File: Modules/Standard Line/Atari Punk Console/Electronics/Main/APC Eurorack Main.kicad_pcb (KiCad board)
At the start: 2 copper layers, 26 x 110 mm, 24 parts, among them IC1 78L05, IC2 LM556, J1 Power, J4 CV2, J5 Out, J6 CV1

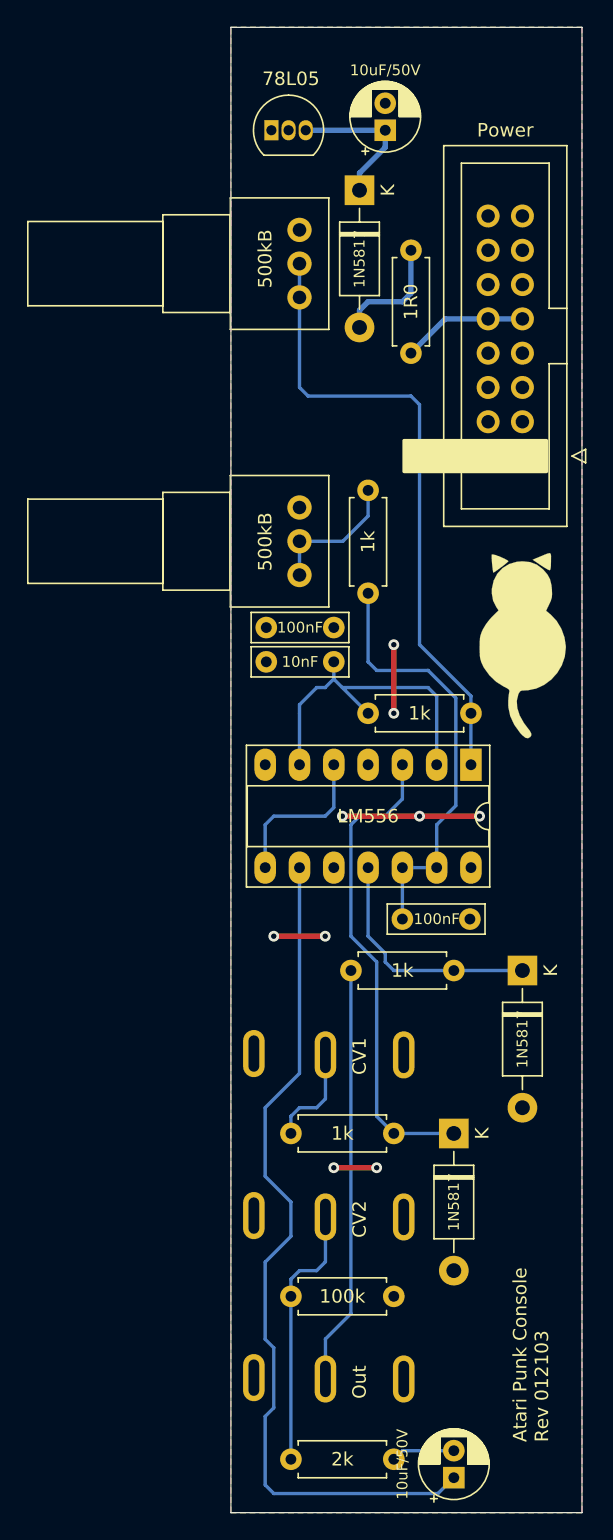
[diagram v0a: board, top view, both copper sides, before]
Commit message: 4Ch Mixer added
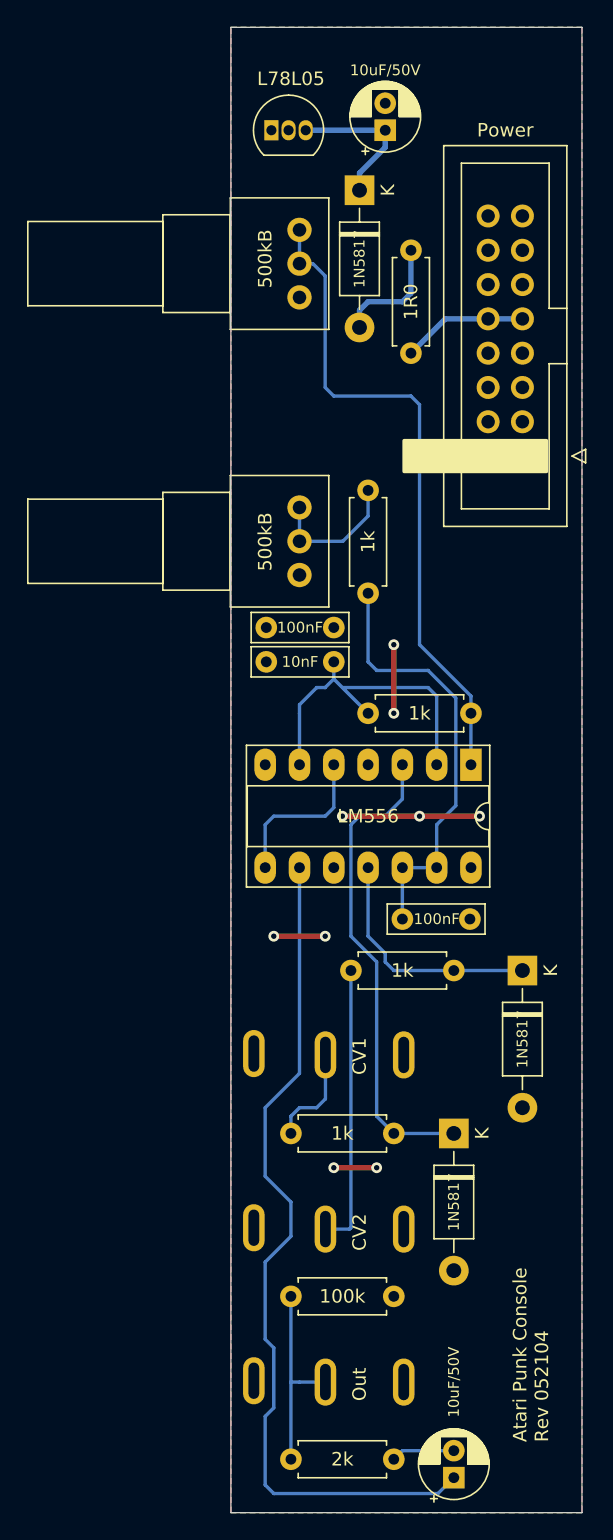
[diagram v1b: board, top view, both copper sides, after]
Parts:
- removed G***: LOGO, Logos:CATs Small
- IC1: value 78L05 -> L78L05
- J4: value CV2 -> Out
- J5: value Out -> CV2
- moved J4 12.2 mm to (0.00, 100.2)
- moved J5 11.1 mm to (0.00, 88.9)
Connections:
- R10 pad 1: +VDC -> Net-(IC2-Pad1)
- R10 pad 3: Net-(IC2-Pad1) -> +VDC
- R11 pad 1: +VDC -> Net-(R11-Pad1)
- R11 pad 2: Net-(R11-Pad2) -> Net-(R11-Pad1)
- R11 pad 3: Net-(R11-Pad2) -> +VDC
- R9 pad 2: Net-(R11-Pad2) -> Net-(R11-Pad1)
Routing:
- net Net-(R11-Pad2): track 10.3 -> 0.00 mm
- net Net-(R11-Pad1): track 0.00 -> 10.3 mm
- net Net-(J5-PadT): track 31.0 -> 21.0 mm
- net Net-(J4-PadT): track 19.7 -> 14.6 mm
- net Net-(IC2-Pad1): track 46.8 -> 48.8 mm
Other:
- board text added: "Atari Punk Console Rev 052104"
- board text removed: "Atari Punk Console Rev 012103"
